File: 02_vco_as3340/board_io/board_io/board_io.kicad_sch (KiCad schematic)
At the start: 14 parts, among them J1 Tuning RVs, J12 Mode Switch, J13 Power, J15 SYNC MODE, J2 PWM offset, J3 FM CV LVL, J4 PWM CV LVL, SW2 SW_SPDT

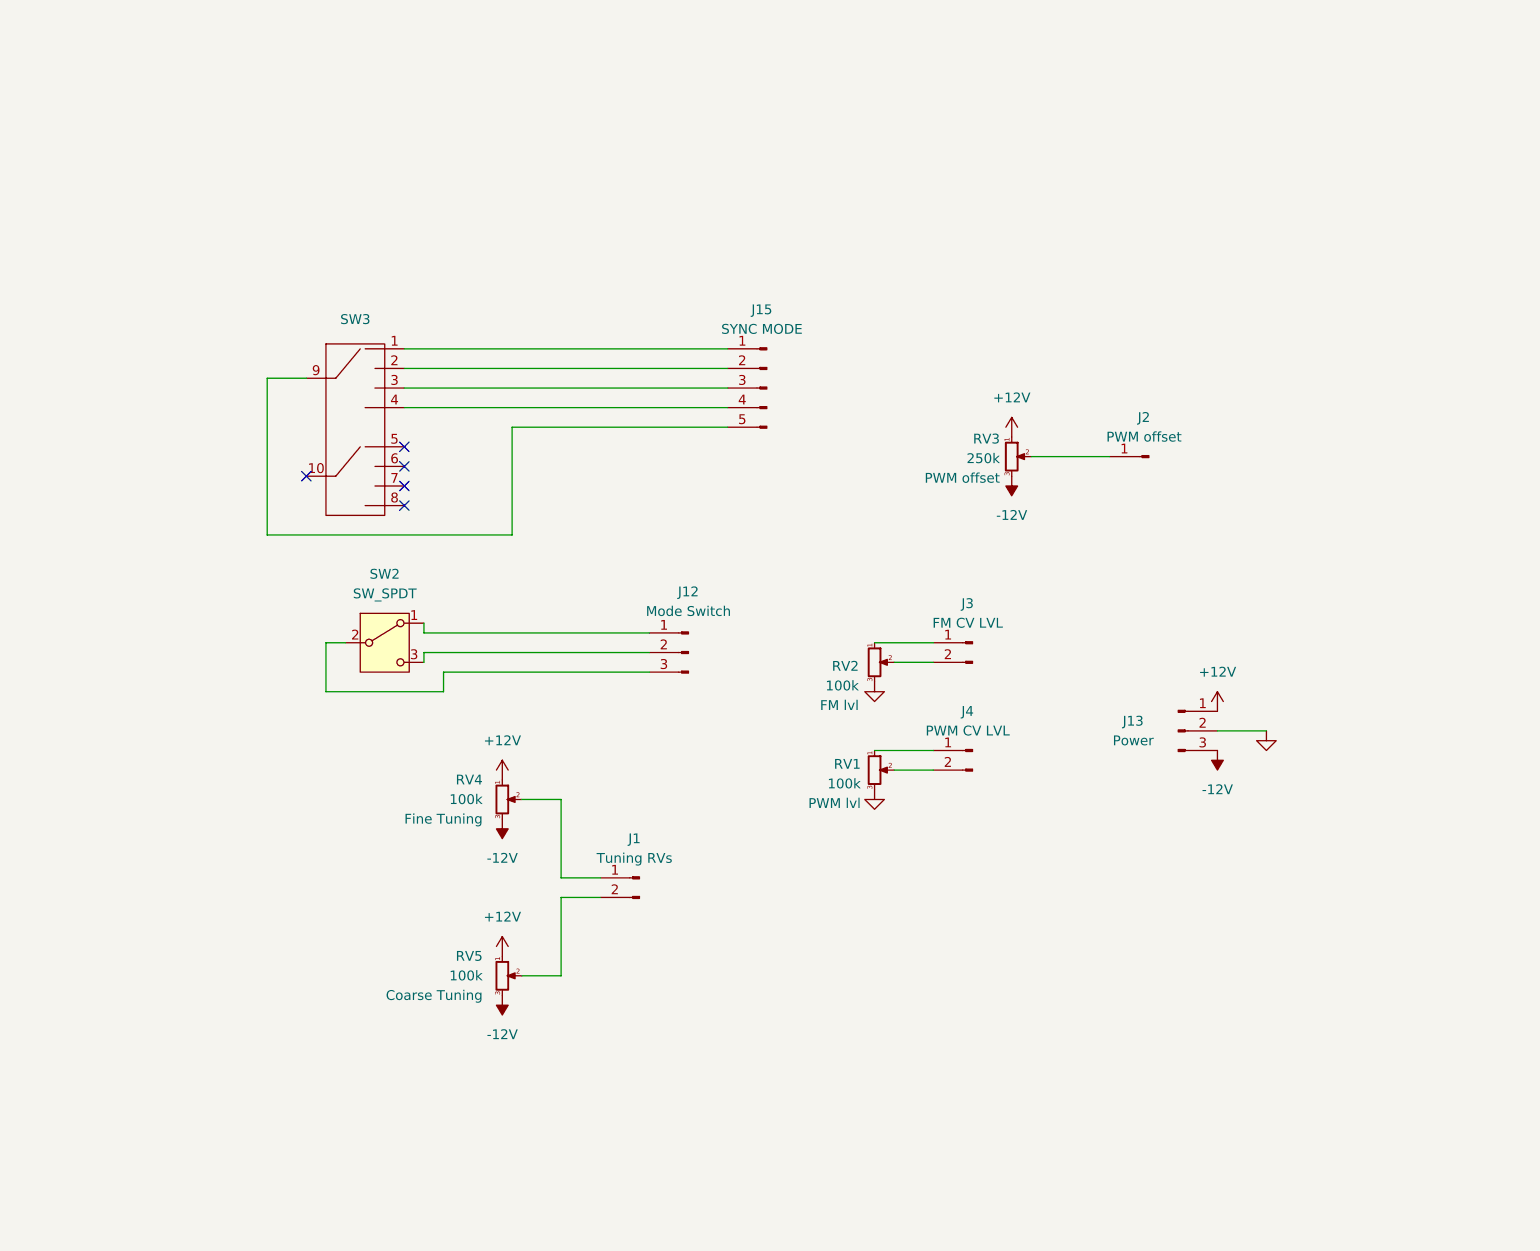
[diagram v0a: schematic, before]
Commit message: made sub board for 02
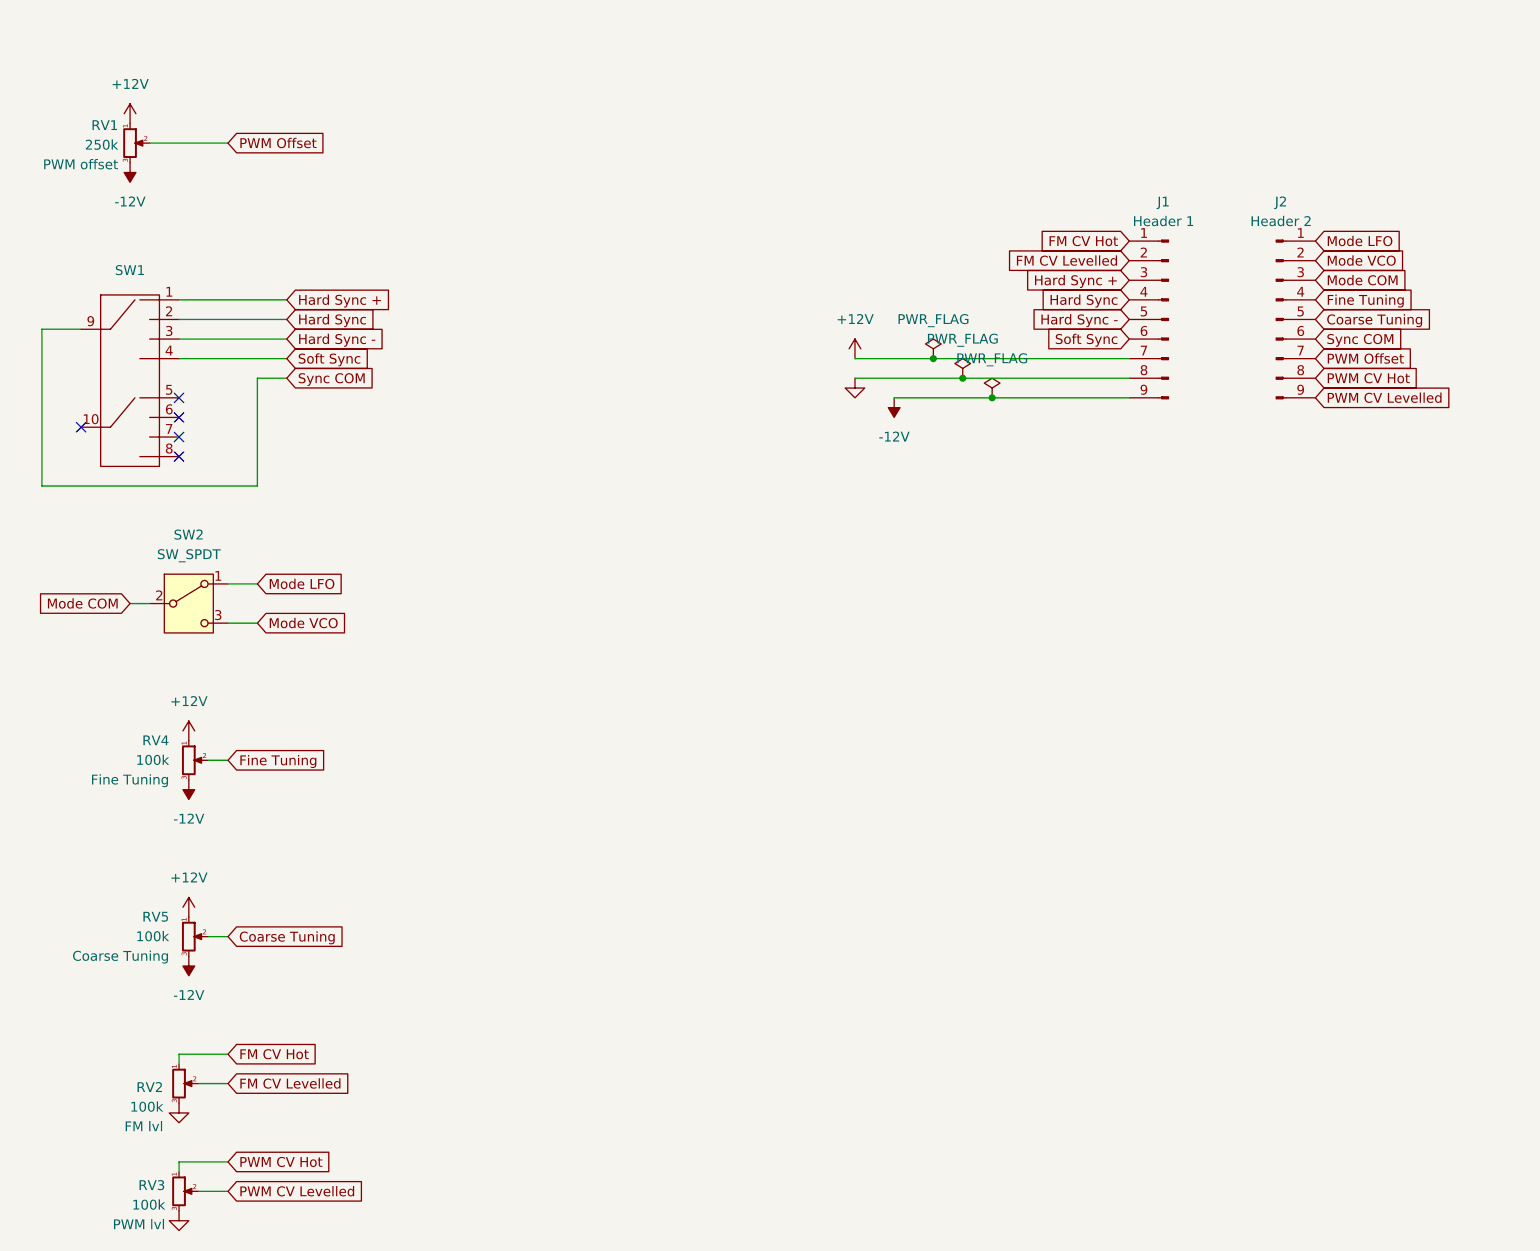
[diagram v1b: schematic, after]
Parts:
- removed J1: Tuning RVs, Connector_PinHeader_2.54mm:PinHeader_1x02_P2.54mm_Vertical, symbol Connector:Conn_01x02_Pin
- removed J12: Mode Switch, Connector_PinHeader_2.54mm:PinHeader_1x03_P2.54mm_Vertical, symbol Connector:Conn_01x03_Pin
- removed J13: Power, Connector_PinHeader_2.54mm:PinHeader_1x03_P2.54mm_Vertical, symbol Connector:Conn_01x03_Pin
- removed J15: SYNC MODE, Connector_PinHeader_2.54mm:PinHeader_1x05_P2.54mm_Vertical, symbol Connector:Conn_01x05_Pin
- removed J2: PWM offset, Connector_PinHeader_2.54mm:PinHeader_1x01_P2.54mm_Vertical, symbol Connector:Conn_01x01_Pin
- removed J3: FM CV LVL, Connector_PinHeader_2.54mm:PinHeader_1x02_P2.54mm_Vertical, symbol Connector:Conn_01x02_Pin
- removed J4: PWM CV LVL, Connector_PinHeader_2.54mm:PinHeader_1x02_P2.54mm_Vertical, symbol Connector:Conn_01x02_Pin
- added J1: Header 1, Connector_PinHeader_2.54mm:PinHeader_1x09_P2.54mm_Vertical, symbol Connector:Conn_01x09_Pin
- added J2: Header 2, Connector_PinHeader_2.54mm:PinHeader_1x09_P2.54mm_Vertical, symbol Connector:Conn_01x09_Pin
- renumbered RV3 to RV1, RV1 to RV3, SW3 to SW1
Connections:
- net +12V: now also J1.7 (Pin_7)
- net -12V: now also J1.9 (Pin_9)
- net GND: now also J1.8 (Pin_8)
- net Hard Sync +: now reaches SW1.1
- net Hard Sync +: now also J1.3 (Pin_3)
- net Hard Sync: now reaches SW1.2
- net Hard Sync: now also J1.4 (Pin_4)
- net Hard Sync -: now reaches SW1.3
- net Hard Sync -: now also J1.5 (Pin_5)
- net Soft Sync: now reaches SW1.4
- net Soft Sync: now also J1.6 (Pin_6)
- net Sync COM: now reaches SW1.9
- net Sync COM: now also J2.6 (Pin_6)
- net Fine Tuning: now reaches RV4.2
- net Fine Tuning: now also J2.4 (Pin_4)
- net Coarse Tuning: now reaches RV5.2
- net Coarse Tuning: now also J2.5 (Pin_5)
- net Mode LFO: now reaches SW2.1 (A)
- net Mode LFO: now also J2.1 (Pin_1)
- net Mode VCO: now reaches SW2.3 (C)
- net Mode VCO: now also J2.2 (Pin_2)
- net Mode COM: now reaches SW2.2 (B)
- net Mode COM: now also J2.3 (Pin_3)
- net PWM CV Hot: now reaches RV3.1
- net PWM CV Hot: now also J2.8 (Pin_8)
- net PWM CV Levelled: now reaches RV3.2
- net PWM CV Levelled: now also J2.9 (Pin_9)
- net FM CV Hot: now reaches RV2.1
- net FM CV Hot: now also J1.1 (Pin_1)
- net FM CV Levelled: now reaches RV2.2
- net FM CV Levelled: now also J1.2 (Pin_2)
- net PWM Offset: now reaches RV1.2
- net PWM Offset: now also J2.7 (Pin_7)
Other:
- moved on the sheet: RV1, RV2, RV3, RV4, RV5, SW1, SW2

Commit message: routed everyting
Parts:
- removed J1: Header 1, Connector_PinHeader_2.54mm:PinHeader_1x09_P2.54mm_Vertical, symbol Connector:Conn_01x09_Pin
- removed J2: Header 2, Connector_PinHeader_2.54mm:PinHeader_1x09_P2.54mm_Vertical, symbol Connector:Conn_01x09_Pin
- added J3: Header 1, Connector_PinHeader_2.54mm:PinHeader_2x05_P2.54mm_Vertical, symbol Connector_Generic:Conn_02x05_Counter_Clockwise
- added J4: Header 2, Connector_PinHeader_2.54mm:PinHeader_2x04_P2.54mm_Vertical, symbol Connector_Generic:Conn_02x04_Counter_Clockwise
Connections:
- net +12V: now also J3.3 (Pin_3)
- net -12V: now also J3.5 (Pin_5)
- net Coarse Tuning: now also J4.4 (Pin_4)
- net FM CV Hot: now also J3.1 (Pin_1)
- net FM CV Levelled: now also J3.2 (Pin_2)
- net Fine Tuning: now also J4.5 (Pin_5)
- net GND: now also J3.4 (Pin_4)
- net Hard Sync: now also J3.9 (Pin_9)
- net Hard Sync +: now also J3.10 (Pin_10)
- net Hard Sync -: now also J3.8 (Pin_8)
- net Mode COM: now also J4.6 (Pin_6)
- net Mode LFO: now also J4.8 (Pin_8)
- net Mode VCO: now also J4.7 (Pin_7)
- net PWM CV Hot: now also J4.2 (Pin_2)
- net PWM CV Levelled: now also J4.3 (Pin_3)
- net PWM Offset: now also J4.1 (Pin_1)
- net Soft Sync: now also J3.7 (Pin_7)
- net Sync COM: now also J3.6 (Pin_6)

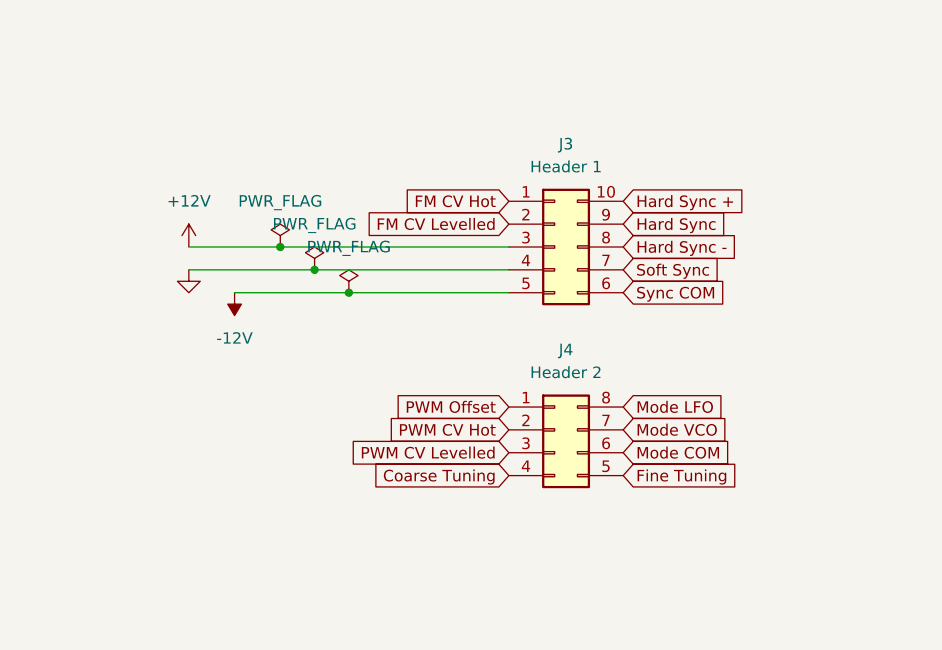
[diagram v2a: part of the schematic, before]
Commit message: fixed layout front/back
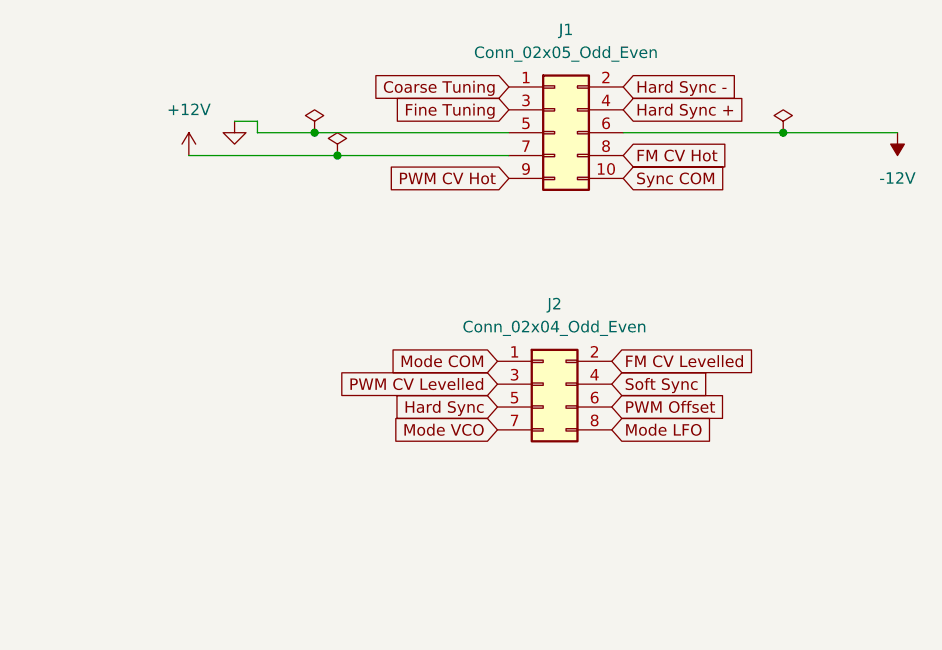
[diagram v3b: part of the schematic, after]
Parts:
- removed J3: Header 1, Connector_PinHeader_2.54mm:PinHeader_2x05_P2.54mm_Vertical, symbol Connector_Generic:Conn_02x05_Counter_Clockwise
- removed J4: Header 2, Connector_PinHeader_2.54mm:PinHeader_2x04_P2.54mm_Vertical, symbol Connector_Generic:Conn_02x04_Counter_Clockwise
- added J1: Conn_02x05_Odd_Even, Connector_PinHeader_2.54mm:PinHeader_2x05_P2.54mm_Vertical, symbol Connector_Generic:Conn_02x05_Odd_Even
- added J2: Conn_02x04_Odd_Even, Connector_PinHeader_2.54mm:PinHeader_2x04_P2.54mm_Vertical, symbol Connector_Generic:Conn_02x04_Odd_Even
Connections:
- net +12V: now also J1.7 (Pin_7)
- net -12V: now also J1.6 (Pin_6)
- net Coarse Tuning: now also J1.1 (Pin_1)
- net FM CV Hot: now also J1.8 (Pin_8)
- net FM CV Levelled: now also J2.2 (Pin_2)
- net Fine Tuning: now also J1.3 (Pin_3)
- net GND: now also J1.5 (Pin_5)
- net Hard Sync: now also J2.5 (Pin_5)
- net Hard Sync +: now also J1.4 (Pin_4)
- net Hard Sync -: now also J1.2 (Pin_2)
- net Mode COM: now also J2.1 (Pin_1)
- net Mode LFO: now also J2.8 (Pin_8)
- net Mode VCO: now also J2.7 (Pin_7)
- net PWM CV Hot: now also J1.9 (Pin_9)
- net PWM CV Levelled: now also J2.3 (Pin_3)
- net PWM Offset: now also J2.6 (Pin_6)
- net Soft Sync: now also J2.4 (Pin_4)
- net Sync COM: now also J1.10 (Pin_10)

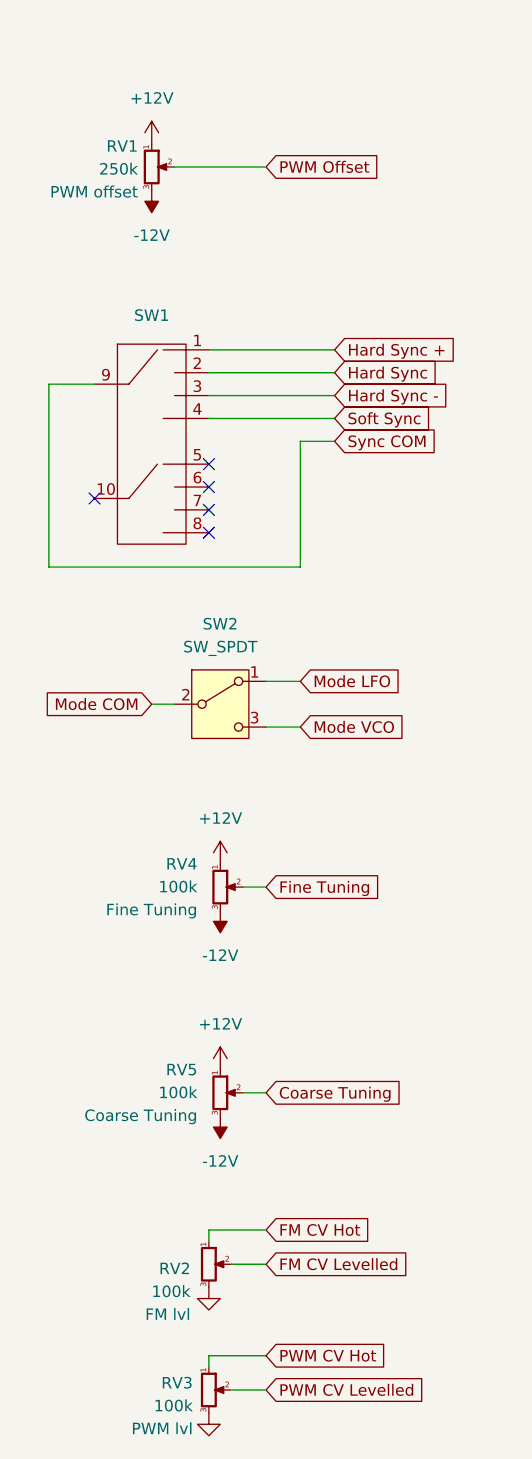
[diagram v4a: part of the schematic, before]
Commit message: fixed potentiometer direction
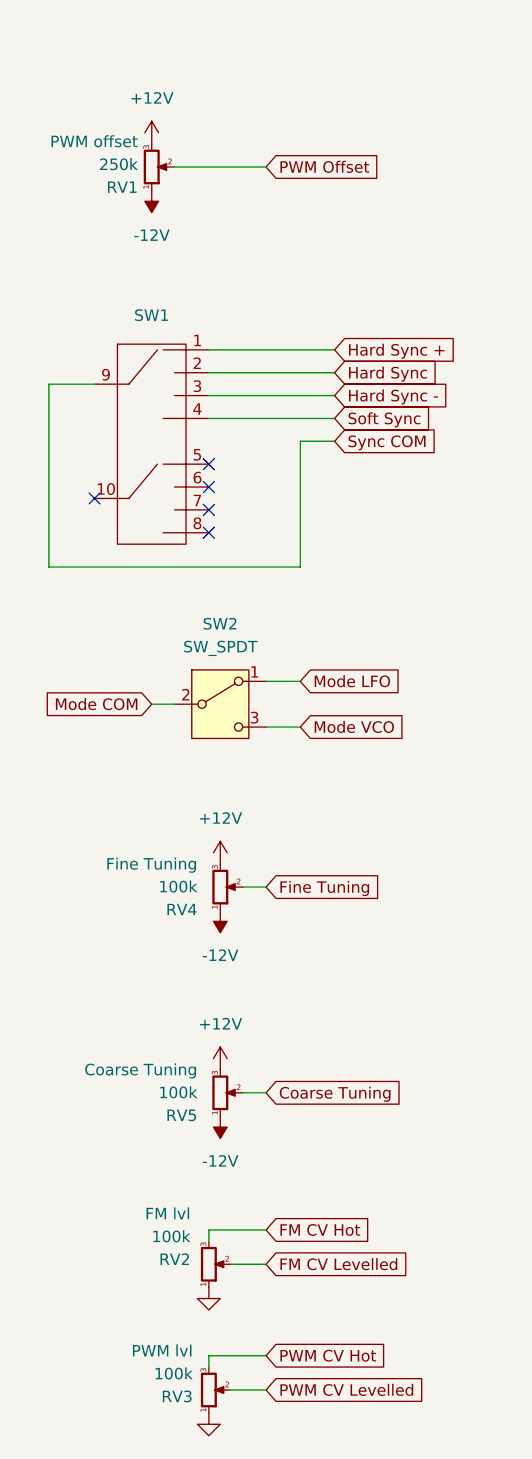
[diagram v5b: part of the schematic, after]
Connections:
- net +12V: now also RV1.3, RV4.3, RV5.3; no longer RV1.1, RV4.1, RV5.1
- net -12V: now also RV1.1, RV4.1, RV5.1; no longer RV1.3, RV4.3, RV5.3
- net FM CV Hot: now also RV2.3; no longer RV2.1
- net GND: now also RV2.1, RV3.1; no longer RV2.3, RV3.3
- net PWM CV Hot: now also RV3.3; no longer RV3.1
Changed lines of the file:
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@@
 		(lib_id "Device:R_Potentiometer_Small")
 		(at 64.77 157.48 0)
+		(mirror x)
 		(unit 1)
 		(exclude_from_sim no)
@@
 		(dnp no)
 		(property "Reference" "RV2"
-			(at 62.738 157.988 0)
+			(at 62.738 156.972 0)
 			(effects
 				(font
@@
 		)
 		(property "Value" "100k"
-			(at 62.738 160.528 0)
+			(at 62.738 154.432 0)
 			(effects
 				(font
@@
 		)
 		(property "Description" "FM lvl"
-			(at 62.738 163.068 0)
+			(at 62.738 151.892 0)
 			(effects
 				(font
@@
 		(lib_id "Device:R_Potentiometer_Small")
 		(at 66.04 138.43 0)
+		(mirror x)
 		(unit 1)
 		(exclude_from_sim no)
@@
 		(fields_autoplaced yes)
 		(property "Reference" "RV5"
-			(at 63.5 135.8899 0)
+			(at 63.5 140.9701 0)
 			(effects
 				(font
@@
 		)
 		(property "Value" "100k"
-			(at 63.5 138.4299 0)
+			(at 63.5 138.4301 0)
 			(effects
 				(font
@@
 		)
 		(property "Description" "Coarse Tuning"
-			(at 63.5 140.9699 0)
+			(at 63.5 135.8901 0)
 			(effects
 				(font
@@
 		(lib_id "Device:R_Potentiometer_Small")
 		(at 64.77 171.45 0)
+		(mirror x)
 		(unit 1)
 		(exclude_from_sim no)
@@
 		(dnp no)
 		(property "Reference" "RV3"
-			(at 62.992 170.688 0)
+			(at 62.992 172.212 0)
 			(effects
 				(font
@@
 		)
 		(property "Value" "100k"
-			(at 62.992 173.228 0)
+			(at 62.992 169.672 0)
 			(effects
 				(font
@@
 		)
 		(property "Description" "PWM lvl"
-			(at 62.992 175.768 0)
+			(at 62.992 167.132 0)
 			(effects
 				(font
@@
 		(lib_id "Device:R_Potentiometer_Small")
 		(at 66.04 115.57 0)
+		(mirror x)
 		(unit 1)
 		(exclude_from_sim no)
@@
 		(fields_autoplaced yes)
 		(property "Reference" "RV4"
-			(at 63.5 113.0299 0)
+			(at 63.5 118.1101 0)
 			(effects
 				(font
@@
 		)
 		(property "Value" "100k"
-			(at 63.5 115.5699 0)
+			(at 63.5 115.5701 0)
 			(effects
 				(font
@@
 		)
 		(property "Description" "Fine Tuning"
-			(at 63.5 118.1099 0)
+			(at 63.5 113.0301 0)
 			(effects
 				(font
@@
 		(lib_id "Device:R_Potentiometer_Small")
 		(at 58.42 35.56 0)
+		(mirror x)
 		(unit 1)
 		(exclude_from_sim no)
@@
 		(dnp no)
 		(property "Reference" "RV1"
-			(at 56.896 33.274 0)
+			(at 56.896 37.846 0)
 			(effects
 				(font
@@
 		)
 		(property "Value" "250k"
-			(at 56.896 35.814 0)
+			(at 56.896 35.306 0)
 			(effects
 				(font
@@
 		)
 		(property "Description" "PWM offset"
-			(at 56.896 38.354 0)
-			(effects
-				(font
+			(at 56.896 32.766 0)
+			(effects
+				(font

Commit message: final tweaks
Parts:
- RV1, RV2, RV3, RV4, RV5: footprint Potentiometer_THT:Potentiometer_Alpha_RD901F-40-00D_Single_Vertical_CircularHoles -> cynthia:pot
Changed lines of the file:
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@@
 			)
 		)
-		(property "Footprint" "Potentiometer_THT:Potentiometer_Alpha_RD901F-40-00D_Single_Vertical_CircularHoles"
+		(property "Footprint" "cynthia:pot"
 			(at 64.77 157.48 0)
 			(effects
@@
 			)
 		)
-		(property "Footprint" "Potentiometer_THT:Potentiometer_Alpha_RD901F-40-00D_Single_Vertical_CircularHoles"
+		(property "Footprint" "cynthia:pot"
 			(at 66.04 138.43 0)
 			(effects
@@
 			)
 		)
-		(property "Footprint" "Potentiometer_THT:Potentiometer_Alpha_RD901F-40-00D_Single_Vertical_CircularHoles"
+		(property "Footprint" "cynthia:pot"
 			(at 64.77 171.45 0)
 			(effects
@@
 			)
 		)
-		(property "Footprint" "Potentiometer_THT:Potentiometer_Alpha_RD901F-40-00D_Single_Vertical_CircularHoles"
+		(property "Footprint" "cynthia:pot"
 			(at 66.04 115.57 0)
 			(effects
@@
 			)
 		)
-		(property "Footprint" "Potentiometer_THT:Potentiometer_Alpha_RD901F-40-00D_Single_Vertical_CircularHoles"
+		(property "Footprint" "cynthia:pot"
 			(at 58.42 35.56 0)
 			(effects
